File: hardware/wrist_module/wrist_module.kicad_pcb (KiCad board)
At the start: 2 copper layers, 59 x 48 mm, 28 parts, among them J1 BATT CONN, J3 MOT 1, J4 MOT 2, J5 MOT 3, J6 MOT 4, J7 MOT 5, SW1 TOGG BTN, SW2 PWR SW, U1 XIAO ESP32C3, U2 ULN2003A

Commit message: Adjustments to Schematics and PCB Layout to Showcase DareDevil Logo
Added the DareDevil Logo to the Schematic, improved the location of the
DareDevil logo on the PCB, re-exported images to reflect changes
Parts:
- moved J1 1.50 mm to (98.0, 77.0)
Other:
- board text added: "+"
- board text added: "-"
- board text added: "DAREDEVIL WRIST MODULE (Rev. A)"
- board text removed: "WRIST MODULE - CSE115A"

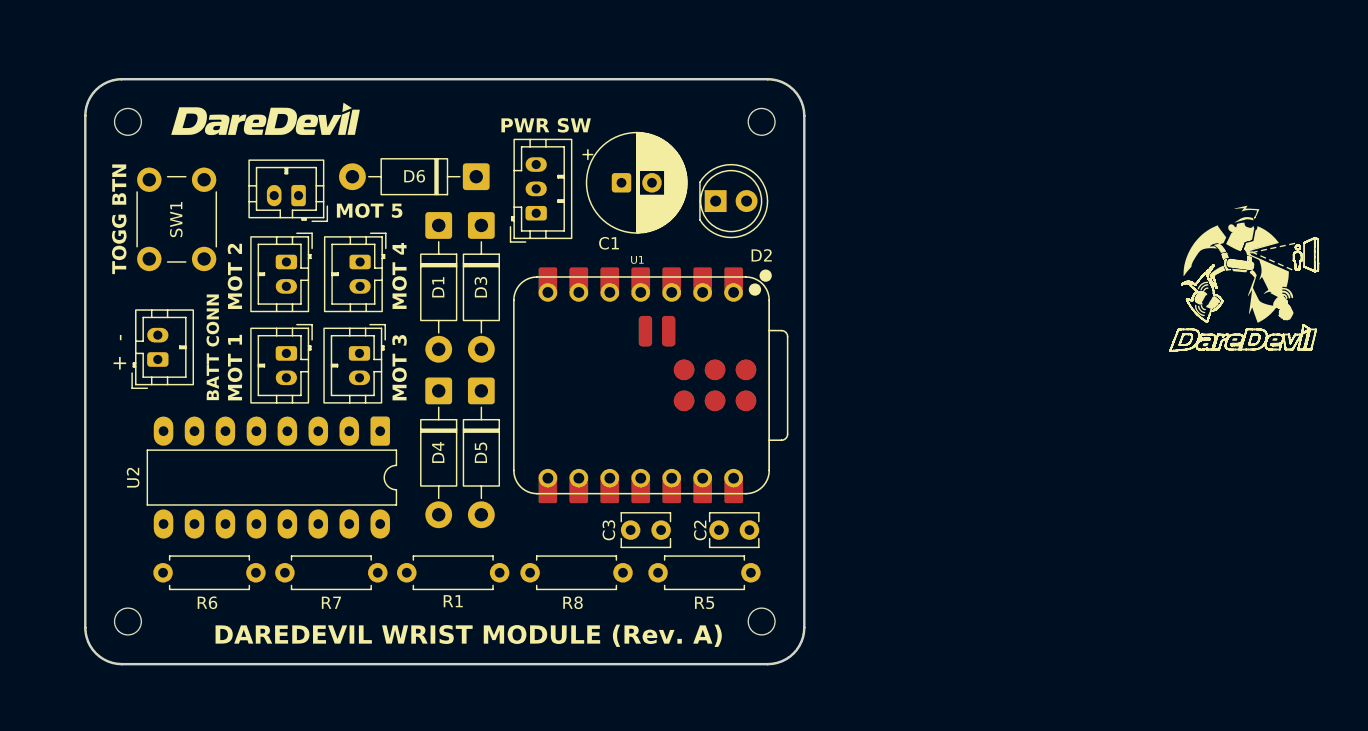
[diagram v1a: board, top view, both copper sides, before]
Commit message: Added traces to PCB, updated READMEs
Successfully routed all traces, added GND netting, closer to
manufacturing.
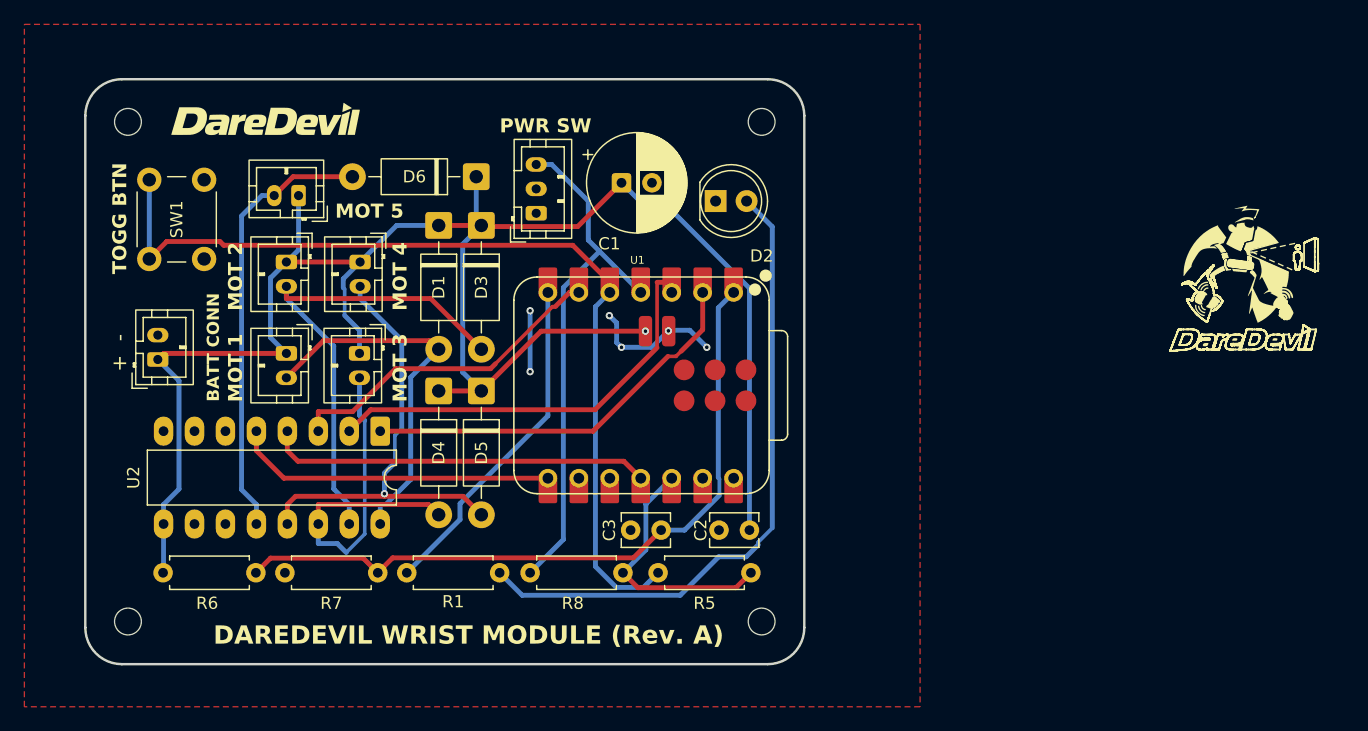
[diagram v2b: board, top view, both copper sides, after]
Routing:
- net +BATT: track 0.00 -> 154.8 mm, vias 0 -> 1
- net Net-(U1-D4): track 0.00 -> 76.4 mm
- net Net-(U1-D0): track 0.00 -> 59.7 mm
- net Net-(D2-A): track 0.00 -> 53.3 mm
- net Net-(SW2-C): track 0.00 -> 44.4 mm
- net /2_OUT: track 0.00 -> 40.4 mm
- net /4_OUT: track 0.00 -> 37.7 mm, vias 0 -> 1
- net /5_OUT: track 0.00 -> 36.2 mm
- net /2_PWM: track 0.00 -> 35.5 mm
- net /1_PWM: track 0.00 -> 33.8 mm
- net /4_PWM: track 0.00 -> 32.4 mm
- net /3_OUT: track 0.00 -> 31.2 mm
- net /1_OUT: track 0.00 -> 30.7 mm
- net Net-(U1-TX_D6): track 0.00 -> 28.6 mm
- net /3_PWM: track 0.00 -> 27.9 mm
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- added copper zone on F.Cu, net GND

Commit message: Added Battery Test Points
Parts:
- added T1: TestPoint_THTPad_1.5x1.5mm_Drill0.7mm, TestPoint:TestPoint_THTPad_1.5x1.5mm_Drill0.7mm, F.Cu at (94.0, 77.8)
- added T2: TestPoint_THTPad_D1.5mm_Drill0.7mm, TestPoint:TestPoint_THTPad_D1.5mm_Drill0.7mm, F.Cu at (94.0, 74.5)
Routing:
- net +BATT: track 154.8 -> 159.6 mm
